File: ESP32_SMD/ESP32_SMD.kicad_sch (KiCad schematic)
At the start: 25 parts, among them J1 Conn_01x02_Socket, J10 Conn_01x02_Socket, J11 Conn_01x15_Socket, J12 Conn_01x02_Socket, J13 Conn_01x02_Socket, J14 Conn_01x02_Socket, J15 Conn_01x02_Socket, J16 Conn_01x02_Socket, J2 Conn_01x02_Socket, J3 Serial Converter, J4 I2C, J5 Conn_01x02_Socket, J6 Conn_01x02_Socket, J7 Conn_01x02_Socket, J8 Conn_01x02_Socket, J9 Conn_01x02_Socket, SW1 SW_Nidec_CAS-120A1, SW2 SW_DPST_x2, SW3 SW_DPST_x2, U1 ESP32-WROOM-32E

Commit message: v1.0.1
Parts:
- SW1: footprint Connector_PinHeader_2.54mm:PinHeader_1x03_P2.54mm_Vertical -> TerminalBlock:TerminalBlock_Xinya_XY308-2.54-3P_1x03_P2.54mm_Horizontal
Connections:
- net at J2.1 (Pin_1), J3.3 (Pin_3), U1.35 (TXD0/IO1): now also J11.7 (Pin_7); no longer J11.2 (Pin_2)
- net at J2.2 (Pin_2), J3.4 (Pin_4), U1.34 (RXD0/IO3): now also J11.6 (Pin_6); no longer J11.4 (Pin_4)
- net at C1.2, J12.2 (Pin_2), SW3.2 (B)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: now also J11.11 (Pin_11); no longer J11.1 (Pin_1)
- net at J6.1 (Pin_1), U1.13 (IO14): now also J11.1 (Pin_1); no longer J11.9 (Pin_9)
- net at J16.1 (Pin_1), U1.37 (IO23): now also J11.8 (Pin_8); no longer J11.15 (Pin_15)
- net at J16.2 (Pin_2), U1.31 (IO19): now also J11.13 (Pin_13); no longer J11.14 (Pin_14)
- net at J12.1 (Pin_1), U1.24 (IO2): now also J11.10 (Pin_10); no longer J11.3 (Pin_3)
- net at J15.1 (Pin_1), U1.30 (IO18): now also J11.5 (Pin_5); no longer J11.13 (Pin_13)
- net at J13.1 (Pin_1), U1.14 (IO12): now also J11.15 (Pin_15); no longer J11.7 (Pin_7)
- net at J13.2 (Pin_2), U1.29 (IO5): now also J11.14 (Pin_14); no longer J11.6 (Pin_6)
- net at J14.1 (Pin_1), U1.27 (IO16): now also J11.4 (Pin_4); no longer J11.11 (Pin_11)
- net at J14.2 (Pin_2), U1.23 (IO15): now also J11.3 (Pin_3); no longer J11.10 (Pin_10)
- new net: J11.2 (Pin_2), J5.1 (Pin_1), U1.16 (IO13)
- new net: J11.9 (Pin_9), J5.2 (Pin_2), U1.26 (IO4)
- no-connect marks 0 -> 1

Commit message: v1.0.0
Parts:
- added J17: I2C, Connector_JST:JST_XH_B2B-XH-A_1x02_P2.50mm_Vertical, symbol Connector:Conn_01x02_Socket
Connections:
- net at C1.2, J11.11 (Pin_11), SW3.2 (B)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: now also J12.1 (Pin_1); no longer J12.2 (Pin_2)
- net at J9.1 (Pin_1): now also U1.4 (SENSOR_VP); no longer U1.5 (SENSOR_VN)
- net at J9.2 (Pin_2): now also U1.5 (SENSOR_VN); no longer U1.4 (SENSOR_VP)
- net at J4.1 (Pin_1), U1.33 (IO21): now also J17.1 (Pin_1)
- net at J4.2 (Pin_2), U1.36 (IO22): now also J17.2 (Pin_2)
- net at J11.10 (Pin_10), U1.24 (IO2): now also J12.2 (Pin_2); no longer J12.1 (Pin_1)
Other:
- moved on the sheet: J9
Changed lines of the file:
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@@
 	(paper "A4")
 	(junction
-		(at 152.4 59.69)
+		(at 190.5 93.98)
 		(diameter 0)
 		(color 0 0 0 0)
@@
 	)
 	(junction
+		(at 190.5 96.52)
+		(diameter 0)
+		(color 0 0 0 0)
+	)
+	(junction
+		(at 151.13 59.69)
+		(diameter 0)
+		(color 0 0 0 0)
+	)
+	(junction
 		(at 177.8 90.17)
 		(diameter 0)
@@
 	)
 	(junction
+		(at 157.48 64.77)
+		(diameter 0)
+		(color 0 0 0 0)
+	)
+	(junction
 		(at 115.57 36.83)
 		(diameter 0)
@@
 	)
 	(junction
-		(at 154.94 64.77)
-		(diameter 0)
-		(color 0 0 0 0)
-	)
-	(junction
 		(at 62.23 24.13)
 		(diameter 0)
@@
 	(wire
 		(pts
-			(xy 152.4 59.69) (xy 193.04 59.69)
-		)
-		(stroke
-			(width 0)
-			(type default)
-		)
-	)
-	(wire
-		(pts
 			(xy 200.66 67.31) (xy 217.17 67.31)
 		)
@@
 	(wire
 		(pts
-			(xy 85.09 63.5) (xy 85.09 64.77)
-		)
-		(stroke
-			(width 0)
-			(type default)
-		)
-	)
-	(wire
-		(pts
 			(xy 228.6 71.12) (xy 237.49 71.12)
 		)
@@
 	(wire
 		(pts
-			(xy 82.55 63.5) (xy 85.09 63.5)
-		)
-		(stroke
-			(width 0)
-			(type default)
-		)
-	)
-	(wire
-		(pts
-			(xy 186.69 96.52) (xy 193.04 96.52)
+			(xy 186.69 96.52) (xy 190.5 96.52)
 		)
 		(stroke
@@
 	(wire
 		(pts
-			(xy 140.97 59.69) (xy 152.4 59.69)
+			(xy 140.97 59.69) (xy 151.13 59.69)
 		)
 		(stroke
@@
 	(wire
 		(pts
+			(xy 190.5 97.79) (xy 204.47 97.79)
+		)
+		(stroke
+			(width 0)
+			(type default)
+		)
+	)
+	(wire
+		(pts
 			(xy 55.88 38.1) (xy 55.88 40.64)
 		)
@@
 	(wire
 		(pts
+			(xy 151.13 59.69) (xy 151.13 142.24)
+		)
+		(stroke
+			(width 0)
+			(type default)
+		)
+	)
+	(wire
+		(pts
 			(xy 212.09 27.94) (xy 212.09 -8.89)
 		)
@@
 	(wire
 		(pts
+			(xy 157.48 64.77) (xy 157.48 144.78)
+		)
+		(stroke
+			(width 0)
+			(type default)
+		)
+	)
+	(wire
+		(pts
 			(xy 195.58 39.37) (xy 261.62 39.37)
 		)
@@
 	(wire
 		(pts
+			(xy 190.5 93.98) (xy 193.04 93.98)
+		)
+		(stroke
+			(width 0)
+			(type default)
+		)
+	)
+	(wire
+		(pts
 			(xy 222.25 69.85) (xy 222.25 66.04)
 		)
@@
 	(wire
 		(pts
-			(xy 154.94 64.77) (xy 154.94 146.05)
+			(xy 130.81 27.94) (xy 130.81 38.1)
 		)
 		(stroke
@@
 	(wire
 		(pts
-			(xy 130.81 27.94) (xy 130.81 38.1)
+			(xy 190.5 95.25) (xy 204.47 95.25)
+		)
+		(stroke
+			(width 0)
+			(type default)
+		)
+	)
+	(wire
+		(pts
+			(xy 157.48 144.78) (xy 152.4 144.78)
 		)
 		(stroke
@@
 	(wire
 		(pts
+			(xy 78.74 64.77) (xy 83.82 64.77)
+		)
+		(stroke
+			(width 0)
+			(type default)
+		)
+	)
+	(wire
+		(pts
 			(xy 204.47 20.32) (xy 208.28 20.32)
 		)
@@
 	(wire
 		(pts
+			(xy 85.09 64.77) (xy 85.09 63.5)
+		)
+		(stroke
+			(width 0)
+			(type default)
+		)
+	)
+	(wire
+		(pts
 			(xy 177.8 90.17) (xy 177.8 146.05)
 		)
@@
 	(wire
 		(pts
+			(xy 83.82 64.77) (xy 83.82 67.31)
+		)
+		(stroke
+			(width 0)
+			(type default)
+		)
+	)
+	(wire
+		(pts
 			(xy 55.88 135.89) (xy 121.92 135.89)
 		)
@@
 	(wire
 		(pts
+			(xy 190.5 96.52) (xy 193.04 96.52)
+		)
+		(stroke
+			(width 0)
+			(type default)
+		)
+	)
+	(wire
+		(pts
 			(xy 184.15 100.33) (xy 184.15 146.05)
 		)
@@
 	(wire
 		(pts
-			(xy 137.16 64.77) (xy 154.94 64.77)
+			(xy 151.13 59.69) (xy 193.04 59.69)
 		)
 		(stroke
@@
 	(wire
 		(pts
-			(xy 152.4 59.69) (xy 152.4 146.05)
+			(xy 137.16 64.77) (xy 157.48 64.77)
 		)
 		(stroke
@@
 	(wire
 		(pts
+			(xy 151.13 142.24) (xy 154.94 142.24)
+		)
+		(stroke
+			(width 0)
+			(type default)
+		)
+	)
+	(wire
+		(pts
 			(xy 55.88 38.1) (xy 128.27 38.1)
 		)
@@
 	(wire
 		(pts
+			(xy 80.01 63.5) (xy 80.01 67.31)
+		)
+		(stroke
+			(width 0)
+			(type default)
+		)
+	)
+	(wire
+		(pts
 			(xy 184.15 27.94) (xy 184.15 -15.24)
 		)
@@
 	(wire
 		(pts
-			(xy 212.09 -8.89) (xy 210.82 -8.89)
+			(xy 80.01 67.31) (xy 78.74 67.31)
 		)
 		(stroke
@@
 	(wire
 		(pts
-			(xy 199.39 27.94) (xy 199.39 -2.54)
+			(xy 212.09 -8.89) (xy 210.82 -8.89)
 		)
 		(stroke
@@
 	(wire
 		(pts
-			(xy 83.82 66.04) (xy 83.82 67.31)
+			(xy 199.39 27.94) (xy 199.39 -2.54)
 		)
 		(stroke
@@
 	(wire
 		(pts
+			(xy 190.5 93.98) (xy 190.5 95.25)
+		)
+		(stroke
+			(width 0)
+			(type default)
+		)
+	)
+	(wire
+		(pts
 			(xy 97.79 50.8) (xy 95.25 50.8)
 		)
@@
 	(wire
 		(pts
-			(xy 82.55 66.04) (xy 83.82 66.04)
+			(xy 190.5 96.52) (xy 190.5 97.79)
 		)
 		(stroke
@@
 	(wire
 		(pts
+			(xy 85.09 63.5) (xy 80.01 63.5)
+		)
+		(stroke
+			(width 0)
+			(type default)
+		)
+	)
+	(wire
+		(pts
 			(xy 210.82 22.86) (xy 210.82 77.47)
 		)
@@
 	(wire
 		(pts
+			(xy 152.4 144.78) (xy 152.4 146.05)
+		)
+		(stroke
+			(width 0)
+			(type default)
+		)
+	)
+	(wire
+		(pts
 			(xy 223.52 -7.62) (xy 223.52 90.17)
 		)
@@
 	(wire
 		(pts
-			(xy 185.42 93.98) (xy 193.04 93.98)
+			(xy 185.42 93.98) (xy 190.5 93.98)
 		)
 		(stroke
@@
 	(wire
 		(pts
+			(xy 154.94 142.24) (xy 154.94 146.05)
+		)
+		(stroke
+			(width 0)
+			(type default)
+		)
+	)
+	(wire
+		(pts
 			(xy 133.35 27.94) (xy 133.35 35.56)
 		)
@@
 	(wire
 		(pts
-			(xy 154.94 64.77) (xy 198.12 64.77)
+			(xy 157.48 64.77) (xy 198.12 64.77)
 		)
 		(stroke
@@
 	(symbol
 		(lib_id "Connector:Conn_01x02_Socket")
-		(at 77.47 66.04 180)
+		(at 73.66 67.31 180)
 		(unit 1)
 		(exclude_from_sim no)
@@
 		(fields_autoplaced yes)
 		(property "Reference" "J9"
-			(at 78.105 58.42 0)
+			(at 74.295 59.69 0)
 			(effects
 				(font
@@
 		)
 		(property "Value" "Conn_01x02_Socket"
-			(at 78.105 60.96 0)
+			(at 74.295 62.23 0)
 			(effects
 				(font
@@
 		)
 		(property "Footprint" "Connector_JST:JST_XH_B2B-XH-A_1x02_P2.50mm_Vertical"
-			(at 77.47 66.04 0)
+			(at 73.66 67.31 0)
 			(effects
 				(font
@@
 		)
 		(property "Datasheet" "~"
-			(at 77.47 66.04 0)
+			(at 73.66 67.31 0)
 			(effects
 				(font
@@
 		)
 		(property "Description" "Generic connector, single row, 01x02, script generated"
-			(at 77.47 66.04 0)
+			(at 73.66 67.31 0)
 			(effects
 				(font
@@
 					(unit 1)
 				)
+			)
+		)
+	)
+	(symbol
+		(lib_id "Connector:Conn_01x02_Socket")
+		(at 209.55 95.25 0)
+		(unit 1)
+		(exclude_from_sim no)
+		(in_bom yes)
+		(on_board yes)
+		(dnp no)
+		(fields_autoplaced yes)
+		(property "Reference" "J17"
+			(at 210.82 95.2499 0)
+			(effects
+				(font
+					(size 1.27 1.27)
+				)
+				(justify left)
+			)
+		)
+		(property "Value" "I2C"
+			(at 210.82 97.7899 0)
+			(effects
+				(font
+					(size 1.27 1.27)
+				)
+				(justify left)
+			)
+		)
+		(property "Footprint" "Connector_JST:JST_XH_B2B-XH-A_1x02_P2.50mm_Vertical"
+			(at 209.55 95.25 0)
+			(effects
+				(font
+					(size 1.27 1.27)
+				)
+				(hide yes)
+			)
+		)
+		(property "Datasheet" "~"
+			(at 209.55 95.25 0)
+			(effects
+				(font
+					(size 1.27 1.27)
+				)
+				(hide yes)
+			)
+		)
+		(property "Description" "Generic connector, single row, 01x02, script generated"
+			(at 209.55 95.25 0)
+			(effects
+				(font
+					(size 1.27 1.27)
+				)
+				(hide yes)
+			)
+		)
+		(pin "2"
+		)
+		(pin "1"
+		)
+		(instances
+			(project "ESP32_SMD"
+				(path "/16d7c20d-89b8-473d-a0a1-bcb2e2ab28b6"
+					(reference "J17")
+					(unit 1)
+				)

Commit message: v1.0.0
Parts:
- added J18, J19: Conn_01x03_Socket, Connector_JST:JST_XH_B3B-XH-A_1x03_P2.50mm_Vertical, symbol Connector:Conn_01x03_Socket
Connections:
- net at C1.2, J11.11 (Pin_11), J12.1 (Pin_1)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: now also J18.3 (Pin_3)
- net at J11.12 (Pin_12), J15.2 (Pin_2), U1.28 (IO17): now also J19.1 (Pin_1)
- net at J11.14 (Pin_14), J13.2 (Pin_2), U1.29 (IO5): now also J18.2 (Pin_2)
- net at J11.15 (Pin_15), J13.1 (Pin_1), U1.14 (IO12): now also J19.2 (Pin_2)
- net at J11.4 (Pin_4), J14.1 (Pin_1), U1.27 (IO16): now also J19.3 (Pin_3)
- net at J11.5 (Pin_5), J15.1 (Pin_1), U1.30 (IO18): now also J18.1 (Pin_1)

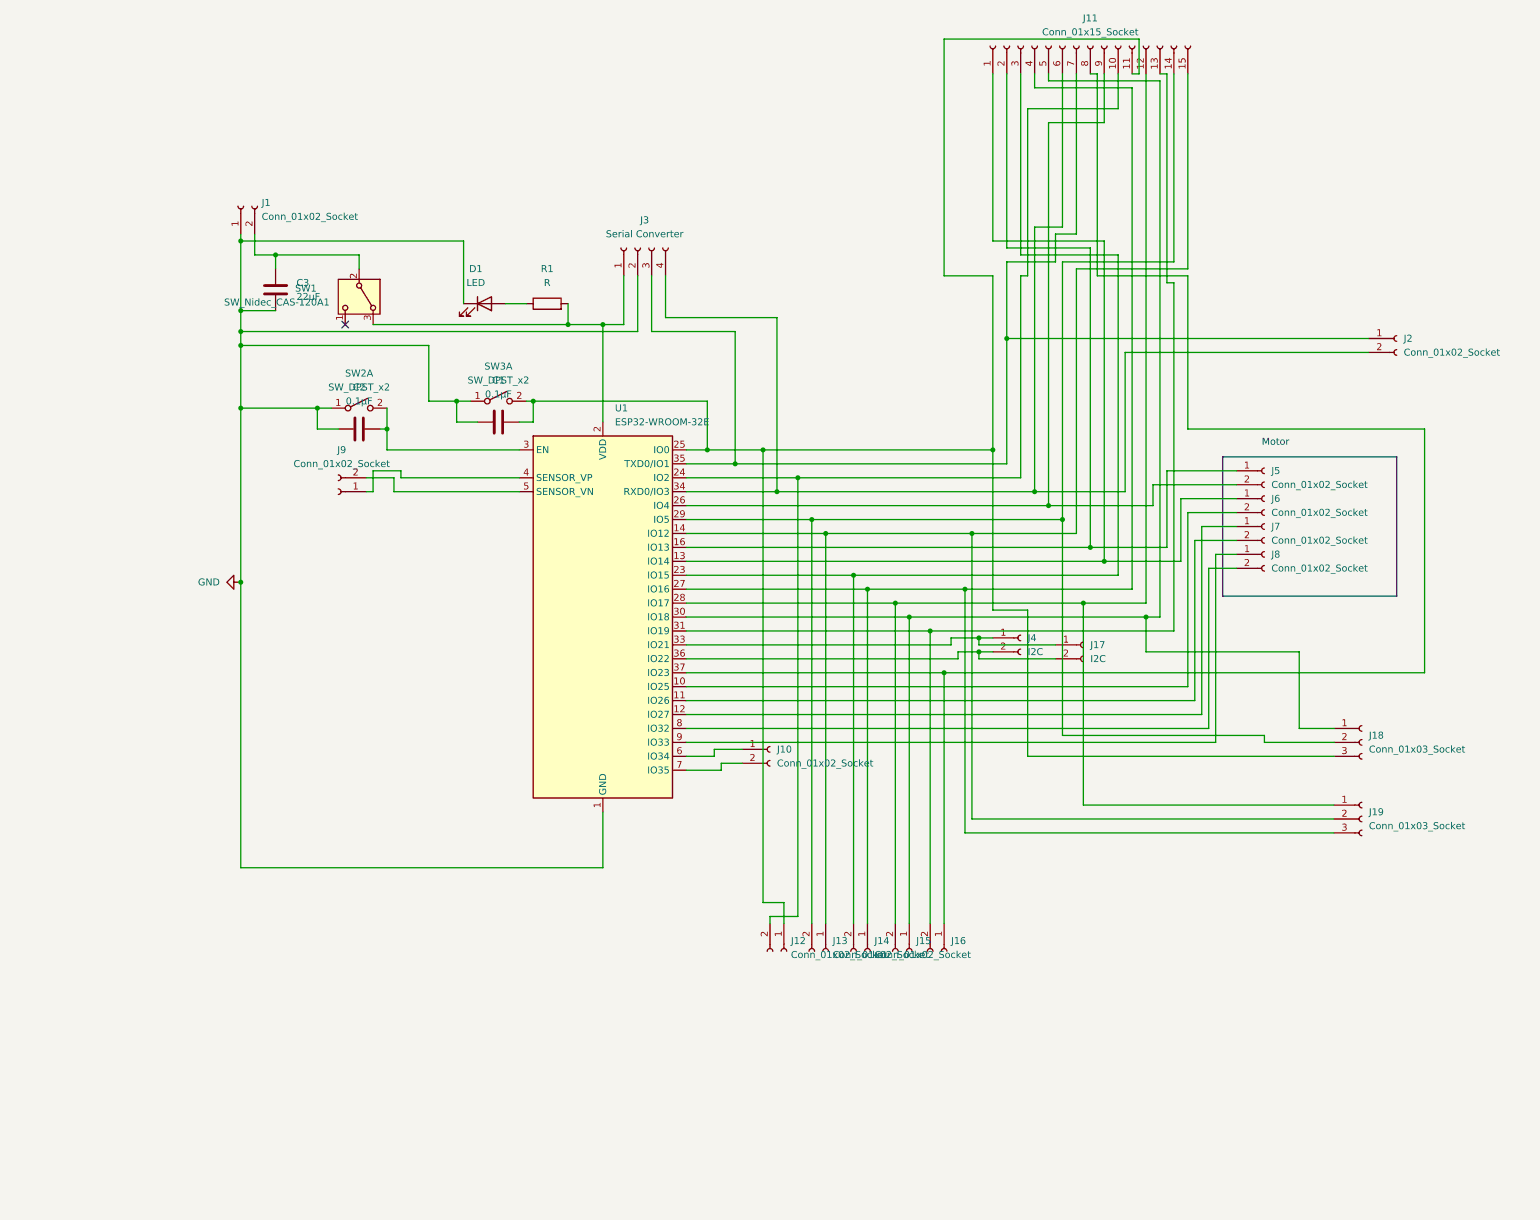
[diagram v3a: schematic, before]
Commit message: v1.1.0
・3端子レギュレータを追加
・ポリスイッチを追加
・配線を改良
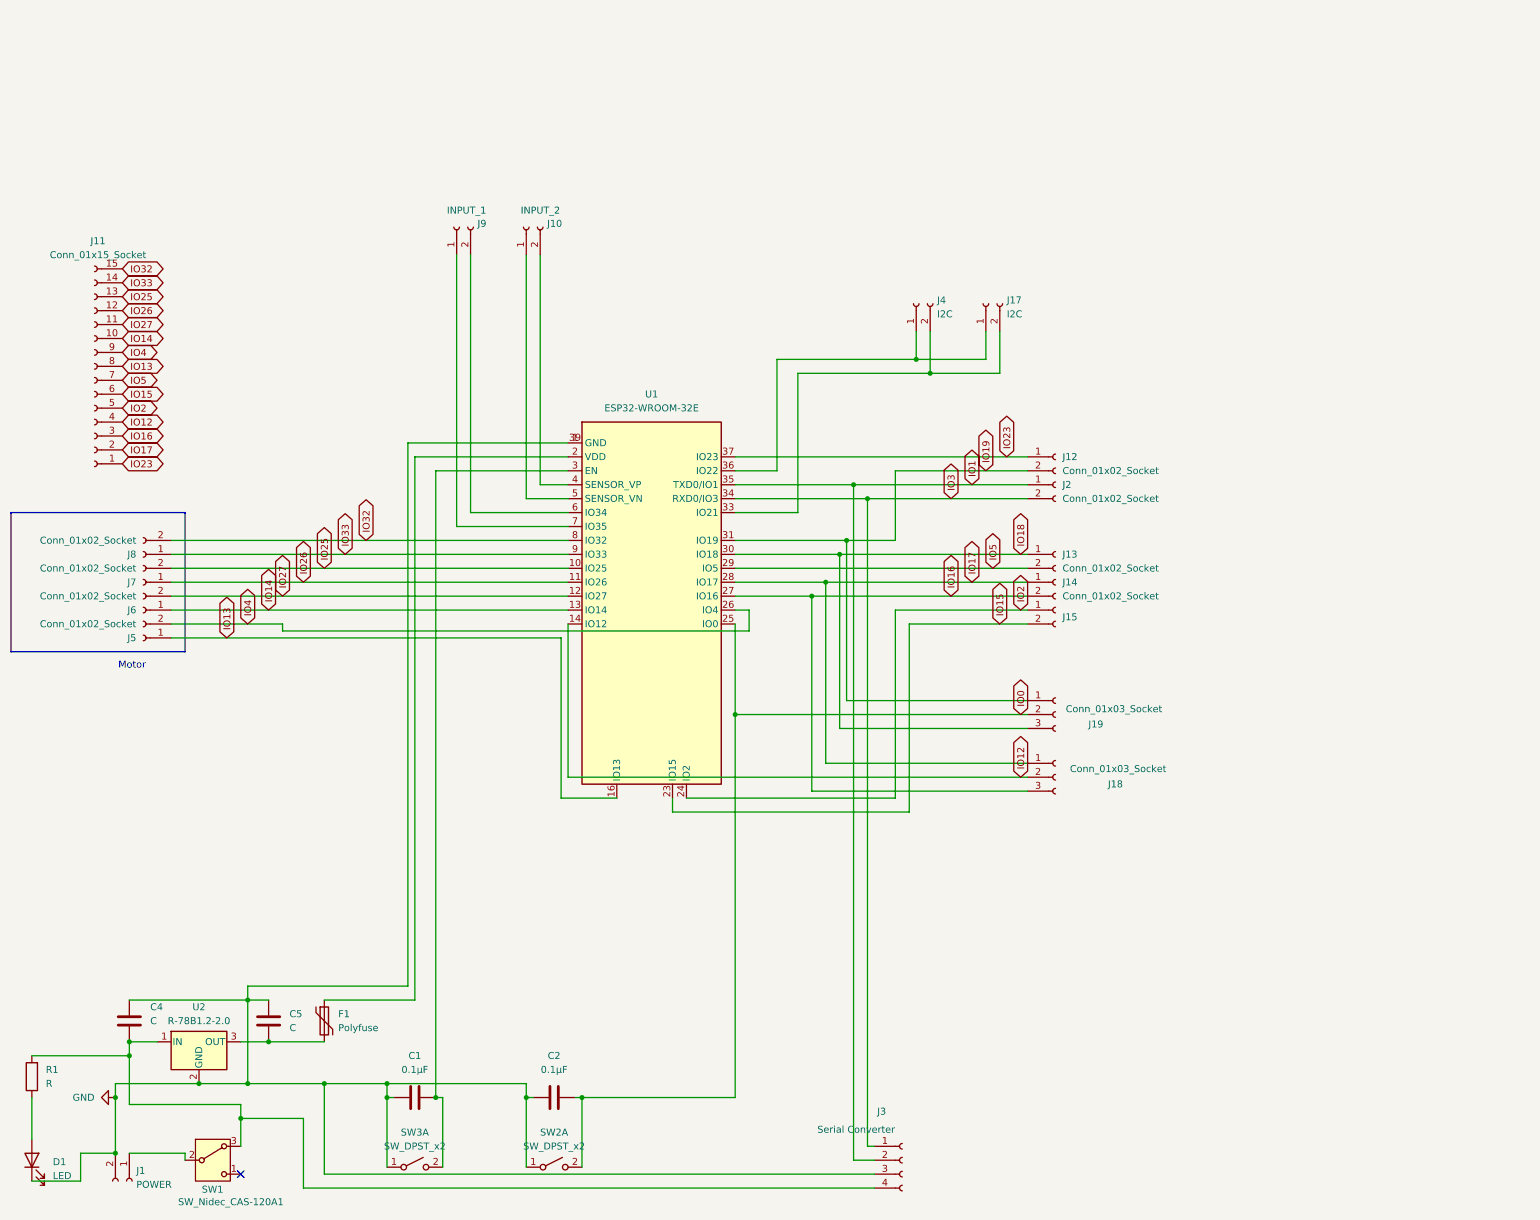
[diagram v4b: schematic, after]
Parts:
- removed C3: 22uF, Capacitor_THT:C_Disc_D3.0mm_W2.0mm_P2.50mm, symbol Device:C
- removed J16: Conn_01x02_Socket, Connector_JST:JST_XH_B2B-XH-A_1x02_P2.50mm_Vertical, symbol Connector:Conn_01x02_Socket
- added C4, C5: C, Connector_PinHeader_2.54mm:PinHeader_1x02_P2.54mm_Vertical, symbol Device:C
- added F1: Polyfuse, 00a:RXEF005, symbol Device:Polyfuse
- added U2: R-78B1.2-2.0, Converter_DCDC:Converter_DCDC_RECOM_R-78B-2.0_THT, symbol Regulator_Switching:R-78B1.2-2.0
- J1: value Conn_01x02_Socket -> POWER
- J10: value Conn_01x02_Socket -> INPUT_2
- J9: value Conn_01x02_Socket -> INPUT_1
- SW2, SW3: footprint 00b:DTS-63 -> 00a:DTS-63-N-V
- U1: footprint RF_Module:ESP32-WROOM-32D -> 00a:ESP32-WROOM-32E; symbol RF_Module:ESP32-WROOM-32E -> 00_a:ESP32-WROOM-32E
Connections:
- net GND: now also C1.2, C2.2, J1.2 (Pin_2), J3.3 (Pin_3), C4.2, C5.2, U2.2 (GND); no longer C1.1, C2.1, J1.1 (Pin_1), J3.2 (Pin_2)
- net at R1.2, SW1.3 (A): now also J3.4 (Pin_4), C4.1, U2.1 (IN); no longer J3.1 (Pin_1), U1.2 (VDD)
- net IO1: now reaches J2.1 (Pin_1), U1.35 (TXD0/IO1)
- net IO1: now also J3.2 (Pin_2); no longer J11.7 (Pin_7), J3.3 (Pin_3)
- net IO3: now reaches J2.2 (Pin_2), U1.34 (RXD0/IO3)
- net IO3: now also J3.1 (Pin_1); no longer J11.6 (Pin_6), J3.4 (Pin_4)
- net at J9.1 (Pin_1): now also U1.7 (IO35); no longer U1.4 (SENSOR_VP)
- net at J9.2 (Pin_2): now also U1.6 (IO34); no longer U1.5 (SENSOR_VN)
- net IO14: now reaches J6.1 (Pin_1), U1.13 (IO14)
- net IO14: now also J11.10 (Pin_10); no longer J11.1 (Pin_1)
- net IO25: now reaches U1.10 (IO25)
- net IO25: now also J11.13 (Pin_13), J7.2 (Pin_2); no longer J6.2 (Pin_2)
- net IO33: now reaches J8.1 (Pin_1), U1.9 (IO33)
- net IO33: now also J11.14 (Pin_14)
- net IO32: now reaches J8.2 (Pin_2), U1.8 (IO32)
- net IO32: now also J11.15 (Pin_15)
- net at J17.1 (Pin_1), J4.1 (Pin_1): now also U1.36 (IO22); no longer U1.33 (IO21)
- net at J17.2 (Pin_2), J4.2 (Pin_2): now also U1.33 (IO21); no longer U1.36 (IO22)
- net IO19: now reaches U1.31 (IO19)
- net IO19: now also J12.2 (Pin_2), J19.1 (Pin_1); no longer J11.13 (Pin_13)
- net IO5: now reaches J13.2 (Pin_2), U1.29 (IO5)
- net IO5: now also J11.7 (Pin_7); no longer J11.14 (Pin_14), J18.2 (Pin_2)
- net IO13: now reaches J5.1 (Pin_1), U1.16 (IO13)
- net IO13: now also J11.8 (Pin_8); no longer J11.2 (Pin_2)
- net IO16: now reaches J11.3 (Pin_3), J14.2 (Pin_2)
- net IO16: now also J18.3 (Pin_3), U1.27 (IO16); no longer U1.23 (IO15)
- net IO2: now reaches J11.5 (Pin_5), J15.1 (Pin_1)
- net IO2: now also U1.24 (IO2); no longer J18.1 (Pin_1), U1.30 (IO18)
- net IO23: now reaches U1.37 (IO23)
- net IO23: now also J11.1 (Pin_1), J12.1 (Pin_1); no longer J11.8 (Pin_8)
- net IO4: now reaches J11.9 (Pin_9), J5.2 (Pin_2), U1.26 (IO4)
- net at J10.1 (Pin_1): now also U1.5 (SENSOR_VN); no longer U1.6 (IO34)
- net at J10.2 (Pin_2): now also U1.4 (SENSOR_VP); no longer U1.7 (IO35)
- net at SW1.2 (B): now also J1.1 (Pin_1); no longer J1.2 (Pin_2)
- net IO26: now reaches J7.1 (Pin_1)
- net IO26: now also J11.12 (Pin_12), U1.11 (IO26); no longer U1.12 (IO27)
- new net: C1.1, SW3.2 (B), U1.3 (EN)
- new net: C5.1, F1.2, U2.3 (OUT)
- new net: F1.1, U1.2 (VDD)
- new net IO0: C2.1, J19.2 (Pin_2), SW2.2 (B), U1.25 (IO0)
- new net IO12: J11.4 (Pin_4), J18.2 (Pin_2), U1.14 (IO12)
- new net IO15: J11.6 (Pin_6), J15.2 (Pin_2), U1.23 (IO15)
- new net IO17: J11.2 (Pin_2), J14.1 (Pin_1), J18.1 (Pin_1), U1.28 (IO17)
- new net IO18: J13.1 (Pin_1), J19.3 (Pin_3), U1.30 (IO18)
- new net IO27: J11.11 (Pin_11), J6.2 (Pin_2), U1.12 (IO27)
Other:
- moved on the sheet: C1, C2, D1, J1, J10, J11, J12, J13, J14, J15, J17, J18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
